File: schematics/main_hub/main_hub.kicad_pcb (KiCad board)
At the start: 2 copper layers, 23 parts, among them J1 Conn_02x25_Counter_Clockwise, J2 Conn_02x25_Counter_Clockwise, J3 Conn_02x25_Counter_Clockwise, J4 Conn_02x25_Counter_Clockwise

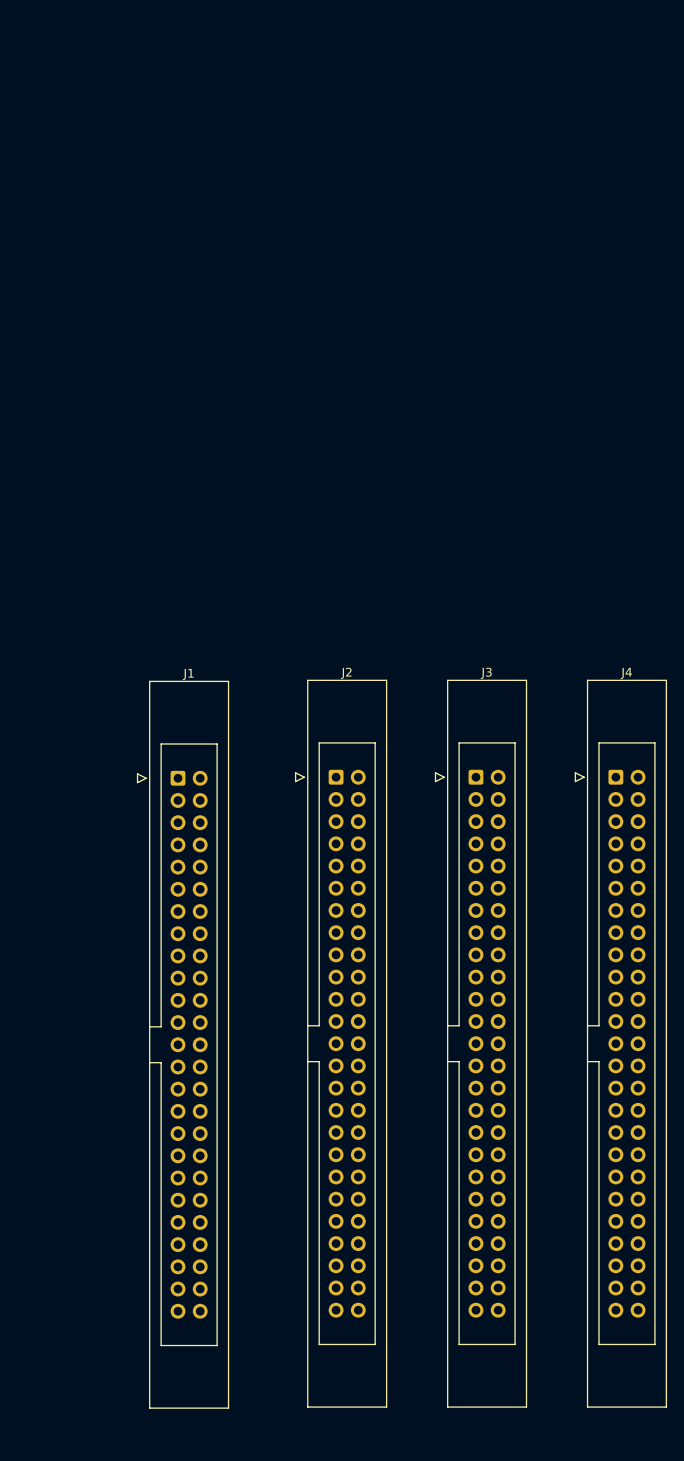
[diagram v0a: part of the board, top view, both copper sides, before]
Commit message: Add more labels to main hub decoder
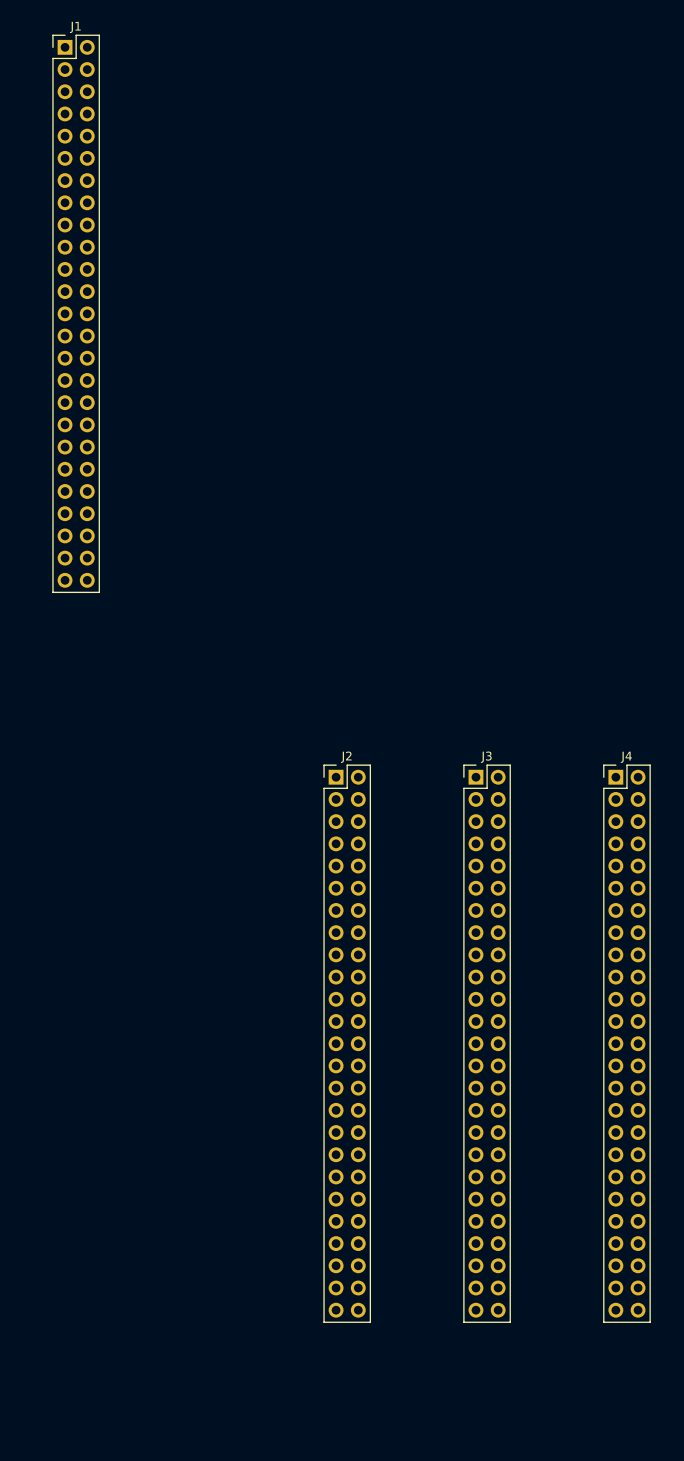
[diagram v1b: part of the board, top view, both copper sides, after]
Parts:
- J1, J2, J3, J4: footprint Connector_IDC:IDC-Header_2x25_P2.54mm_Latch_Vertical -> Connector_PinHeader_2.54mm:PinHeader_2x25_P2.54mm_Vertical
- moved J1 84.6 mm to (180.0, -5.48)
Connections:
- DECODER1 pad 7: unconnected-(DECODER1-S6-Pad7) -> /~{TemporaryHighReader}
- DECODER1 pad 9: unconnected-(DECODER1-S8-Pad9) -> /~{AccumReader}
- DECODER3 pad 7: unconnected-(DECODER3-S6-Pad7) -> /~{TemporaryHighWriter}
- DECODER3 pad 9: unconnected-(DECODER3-S8-Pad9) -> /~{AccumWriter}
- DECODER4 pad 1: unconnected-(DECODER4-S0-Pad1) -> /~{ALUWriter}
- J1 pad 1: /~{Halt} -> VCC
- J1 pad 10: unconnected-(J1-Pin_10-Pad10) -> GND
- J1 pad 2: VCC -> GND
- J1 pad 26: unconnected-(J1-Pin_26-Pad26) -> VCC
- J1 pad 27: unconnected-(J1-Pin_27-Pad27) -> /AccumWriter
- J1 pad 28: unconnected-(J1-Pin_28-Pad28) -> /AccumShiftRight
- J1 pad 29: unconnected-(J1-Pin_29-Pad29) -> /AccumShiftLeft
- J1 pad 3: /~{Reset} -> /~{Clk}
- J1 pad 30: unconnected-(J1-Pin_30-Pad30) -> /~{ALUCarryIn}
- J1 pad 31: unconnected-(J1-Pin_31-Pad31) -> /ALUM
- J1 pad 32: unconnected-(J1-Pin_32-Pad32) -> /ALUS3
- J1 pad 33: unconnected-(J1-Pin_33-Pad33) -> /ALUS2
- J1 pad 34: unconnected-(J1-Pin_34-Pad34) -> /ALUS1
- J1 pad 35: unconnected-(J1-Pin_35-Pad35) -> /ALUS0
- J1 pad 36: unconnected-(J1-Pin_36-Pad36) -> /ALUZeroOut
- J1 pad 37: unconnected-(J1-Pin_37-Pad37) -> /~{ALUCarryOut}
- J1 pad 38: unconnected-(J1-Pin_38-Pad38) -> /ALUSignOut
- J1 pad 39: unconnected-(J1-Pin_39-Pad39) -> /~{ALUWriter}
- J1 pad 4: GND -> /Clk
- J1 pad 40: unconnected-(J1-Pin_40-Pad40) -> /TemporaryHighReader
- J1 pad 41: unconnected-(J1-Pin_41-Pad41) -> /~{TemporaryHighWriter}
- J1 pad 46: unconnected-(J1-Pin_46-Pad46) -> /AccumReader
- J1 pad 48: unconnected-(J1-Pin_48-Pad48) -> /Pulse
- J1 pad 49: unconnected-(J1-Pin_49-Pad49) -> GND
- J1 pad 5: /~{Clk} -> unconnected-(J1-Pin_5-Pad5)
- J1 pad 50: unconnected-(J1-Pin_50-Pad50) -> VCC
- J1 pad 6: /Clk -> unconnected-(J1-Pin_6-Pad6)
- J2 pad 1: /~{Halt} -> VCC
- J2 pad 10: unconnected-(J2-Pin_10-Pad10) -> GND
- J2 pad 2: VCC -> GND
- J2 pad 26: unconnected-(J2-Pin_26-Pad26) -> VCC
- J2 pad 3: /~{Reset} -> /~{Clk}
- J2 pad 4: GND -> /Clk
- J2 pad 48: unconnected-(J2-Pin_48-Pad48) -> /Pulse
- J2 pad 49: unconnected-(J2-Pin_49-Pad49) -> GND
- J2 pad 5: /~{Clk} -> unconnected-(J2-Pin_5-Pad5)
- J2 pad 50: unconnected-(J2-Pin_50-Pad50) -> VCC
- J2 pad 6: /Clk -> unconnected-(J2-Pin_6-Pad6)
- J3 pad 1: /~{Halt} -> VCC
- J3 pad 10: unconnected-(J3-Pin_10-Pad10) -> GND
- J3 pad 2: VCC -> GND
- J3 pad 26: unconnected-(J3-Pin_26-Pad26) -> VCC
- J3 pad 3: /~{Reset} -> /~{Clk}
- J3 pad 4: GND -> /Clk
- J3 pad 48: unconnected-(J3-Pin_48-Pad48) -> /Pulse
- J3 pad 49: unconnected-(J3-Pin_49-Pad49) -> GND
- J3 pad 5: /~{Clk} -> unconnected-(J3-Pin_5-Pad5)
- J3 pad 50: unconnected-(J3-Pin_50-Pad50) -> VCC
- J3 pad 6: /Clk -> unconnected-(J3-Pin_6-Pad6)
- J4 pad 1: /~{Halt} -> VCC
- J4 pad 10: unconnected-(J4-Pin_10-Pad10) -> GND
- J4 pad 2: VCC -> GND
- J4 pad 26: unconnected-(J4-Pin_26-Pad26) -> VCC
- J4 pad 3: /~{Reset} -> /~{Clk}
- J4 pad 4: GND -> /Clk
- J4 pad 48: unconnected-(J4-Pin_48-Pad48) -> /Pulse
- J4 pad 49: unconnected-(J4-Pin_49-Pad49) -> GND
- J4 pad 5: /~{Clk} -> unconnected-(J4-Pin_5-Pad5)
- J4 pad 50: unconnected-(J4-Pin_50-Pad50) -> VCC
- J4 pad 6: /Clk -> unconnected-(J4-Pin_6-Pad6)
- NOT2 pad 10: unconnected-(NOT2-Pad10) -> /AccumReader
- NOT2 pad 11: unconnected-(NOT2-Pad11) -> /~{AccumReader}
- NOT2 pad 12: unconnected-(NOT2-Pad12) -> /TemporaryHighReader
- NOT2 pad 13: unconnected-(NOT2-Pad13) -> /~{TemporaryHighReader}
- NOT2 pad 8: unconnected-(NOT2-Pad8) -> /AccumWriter
- NOT2 pad 9: unconnected-(NOT2-Pad9) -> /~{AccumWriter}
- TABLE1 pad 17: Net-(TABLE1-D5) -> /ALUM
- TABLE1 pad 18: Net-(TABLE1-D6) -> /~{ALUCarryIn}
- TABLE2 pad 17: Net-(TABLE1-D5) -> /ALUM
- TABLE2 pad 18: Net-(TABLE1-D6) -> /~{ALUCarryIn}
- TABLE5 pad 11: Net-(TABLE5-D0) -> /ALUS0
- TABLE5 pad 12: Net-(TABLE5-D1) -> /ALUS1
- TABLE5 pad 13: Net-(TABLE5-D2) -> /ALUS2
- TABLE5 pad 15: Net-(TABLE5-D3) -> /ALUS3
- TABLE5 pad 18: Net-(TABLE5-D6) -> /AccumShiftLeft
- TABLE5 pad 19: Net-(TABLE5-D7) -> /AccumShiftRight
- TABLE6 pad 11: Net-(TABLE5-D0) -> /ALUS0
- TABLE6 pad 12: Net-(TABLE5-D1) -> /ALUS1
- TABLE6 pad 13: Net-(TABLE5-D2) -> /ALUS2
- TABLE6 pad 15: Net-(TABLE5-D3) -> /ALUS3
- TABLE6 pad 18: Net-(TABLE5-D6) -> /AccumShiftLeft
- TABLE6 pad 19: Net-(TABLE5-D7) -> /AccumShiftRight
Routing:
- net Net-(TABLE1-D5): track 41.9 -> 0.00 mm
- net /ALUM: track 0.00 -> 41.9 mm
- net Net-(TABLE1-D6): track 41.2 -> 0.00 mm
- net /~{ALUCarryIn}: track 0.00 -> 41.2 mm
- net Net-(TABLE5-D3): track 40.0 -> 0.00 mm
- net /ALUS3: track 0.00 -> 40.0 mm
- net Net-(TABLE5-D0): track 39.7 -> 0.00 mm
- net /ALUS0: track 0.00 -> 39.7 mm
- net Net-(TABLE5-D1): track 39.7 -> 0.00 mm
- net /ALUS1: track 0.00 -> 39.7 mm

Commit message: Connnect all modules together
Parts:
- added U1: 74LS02, Package_DIP:DIP-14_W7.62mm_Socket_LongPads, F.Cu at (111.4, 15.8)
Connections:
- net Net-(TABLE3-D7) renamed /PCIncrement
- net Net-(TABLE5-D4) renamed /SPDecrement
- net Net-(TABLE5-D5) renamed /SPIncrement
- net Net-(TABLE7-D2) renamed /AddrDecrement
- net Net-(TABLE7-D3) renamed /AddrIncrement
- DECODER1 pad 10: unconnected-(DECODER1-S9-Pad10) -> /~{XHReader}
- DECODER1 pad 11: unconnected-(DECODER1-S10-Pad11) -> /~{YLReader}
- DECODER1 pad 13: unconnected-(DECODER1-S11-Pad13) -> /~{YHReader}
- DECODER1 pad 14: unconnected-(DECODER1-S12-Pad14) -> /~{ZLReader}
- DECODER1 pad 15: unconnected-(DECODER1-S13-Pad15) -> /~{ZHReader}
- DECODER1 pad 16: unconnected-(DECODER1-S14-Pad16) -> /~{FlagsReader}
- DECODER1 pad 17: unconnected-(DECODER1-S15-Pad17) -> /~{InstructionReader}
- DECODER1 pad 2: unconnected-(DECODER1-S1-Pad2) -> /~{MemoryReader}
- DECODER1 pad 3: unconnected-(DECODER1-S2-Pad3) -> /~{SPHighReader}
- DECODER1 pad 4: unconnected-(DECODER1-S3-Pad4) -> /~{SPLowReader}
- DECODER1 pad 5: unconnected-(DECODER1-S4-Pad5) -> /~{PCHighReader}
- DECODER1 pad 6: unconnected-(DECODER1-S5-Pad6) -> /~{PCLowReader}
- DECODER1 pad 8: unconnected-(DECODER1-S7-Pad8) -> /~{TemporaryLowReader}
- DECODER2 pad 1: unconnected-(DECODER2-S0-Pad1) -> /~{AddressHighReader}
- DECODER2 pad 2: unconnected-(DECODER2-S1-Pad2) -> /~{AddressLowReader}
- DECODER3 pad 10: unconnected-(DECODER3-S9-Pad10) -> /~{XHWriter}
- DECODER3 pad 11: unconnected-(DECODER3-S10-Pad11) -> /~{YLWriter}
- DECODER3 pad 13: unconnected-(DECODER3-S11-Pad13) -> /~{YHWriter}
- DECODER3 pad 14: unconnected-(DECODER3-S12-Pad14) -> /~{ZLWriter}
- DECODER3 pad 15: unconnected-(DECODER3-S13-Pad15) -> /~{ZHWriter}
- DECODER3 pad 16: unconnected-(DECODER3-S14-Pad16) -> /~{FlagsWriter}
- DECODER3 pad 17: unconnected-(DECODER3-S15-Pad17) -> /~{ConstantWriter}
- DECODER3 pad 2: unconnected-(DECODER3-S1-Pad2) -> /~{MemoryWriter}
- DECODER3 pad 3: unconnected-(DECODER3-S2-Pad3) -> /~{SPHighWriter}
- DECODER3 pad 4: unconnected-(DECODER3-S3-Pad4) -> /~{SPLowWriter}
- DECODER3 pad 5: unconnected-(DECODER3-S4-Pad5) -> /~{PCHighWriter}
- DECODER3 pad 6: unconnected-(DECODER3-S5-Pad6) -> /~{PCLowWriter}
- DECODER3 pad 8: unconnected-(DECODER3-S7-Pad8) -> /~{TemporaryLowWriter}
- DECODER4 pad 2: unconnected-(DECODER4-S1-Pad2) -> /~{IntAck}
- INSTRUCTION1 pad 11: /Clk -> Net-(INSTRUCTION1-Cp)
- J1 pad 27: /AccumWriter -> /~{AccumWriter}
- J1 pad 40: /TemporaryHighReader -> /~{TemporaryHighReader}
- J1 pad 46: /AccumReader -> /~{AccumReader}
- J2 pad 21: unconnected-(J2-Pin_21-Pad21) -> /ALUZeroOut
- J2 pad 22: unconnected-(J2-Pin_22-Pad22) -> /~{ALUCarryOut}
- J2 pad 23: unconnected-(J2-Pin_23-Pad23) -> /ALUSignOut
- J2 pad 28: unconnected-(J2-Pin_28-Pad28) -> /~{FlagsUpdate}
- J2 pad 29: unconnected-(J2-Pin_29-Pad29) -> /~{ZHReader}
- J2 pad 30: unconnected-(J2-Pin_30-Pad30) -> /~{ZLReader}
- J2 pad 31: unconnected-(J2-Pin_31-Pad31) -> /~{YHReader}
- J2 pad 32: unconnected-(J2-Pin_32-Pad32) -> /~{YLReader}
- J2 pad 33: unconnected-(J2-Pin_33-Pad33) -> /~{XHReader}
- J2 pad 34: unconnected-(J2-Pin_34-Pad34) -> /~{FlagsReader}
- J2 pad 35: unconnected-(J2-Pin_35-Pad35) -> /~{ZHWriter}
- J2 pad 36: unconnected-(J2-Pin_36-Pad36) -> /~{ZLWriter}
- J2 pad 37: unconnected-(J2-Pin_37-Pad37) -> /~{YHWriter}
- J2 pad 38: unconnected-(J2-Pin_38-Pad38) -> /~{YLWriter}
- J2 pad 39: unconnected-(J2-Pin_39-Pad39) -> /~{XHWriter}
- J2 pad 40: unconnected-(J2-Pin_40-Pad40) -> /~{FlagsWriter}
- J2 pad 44: unconnected-(J2-Pin_44-Pad44) -> /STATE8
- J2 pad 45: unconnected-(J2-Pin_45-Pad45) -> /STATE9
- J2 pad 46: unconnected-(J2-Pin_46-Pad46) -> /STATE10
- TABLE1 pad 19: Net-(TABLE1-D7) -> /~{FlagsUpdate}
- TABLE2 pad 19: Net-(TABLE1-D7) -> /~{FlagsUpdate}

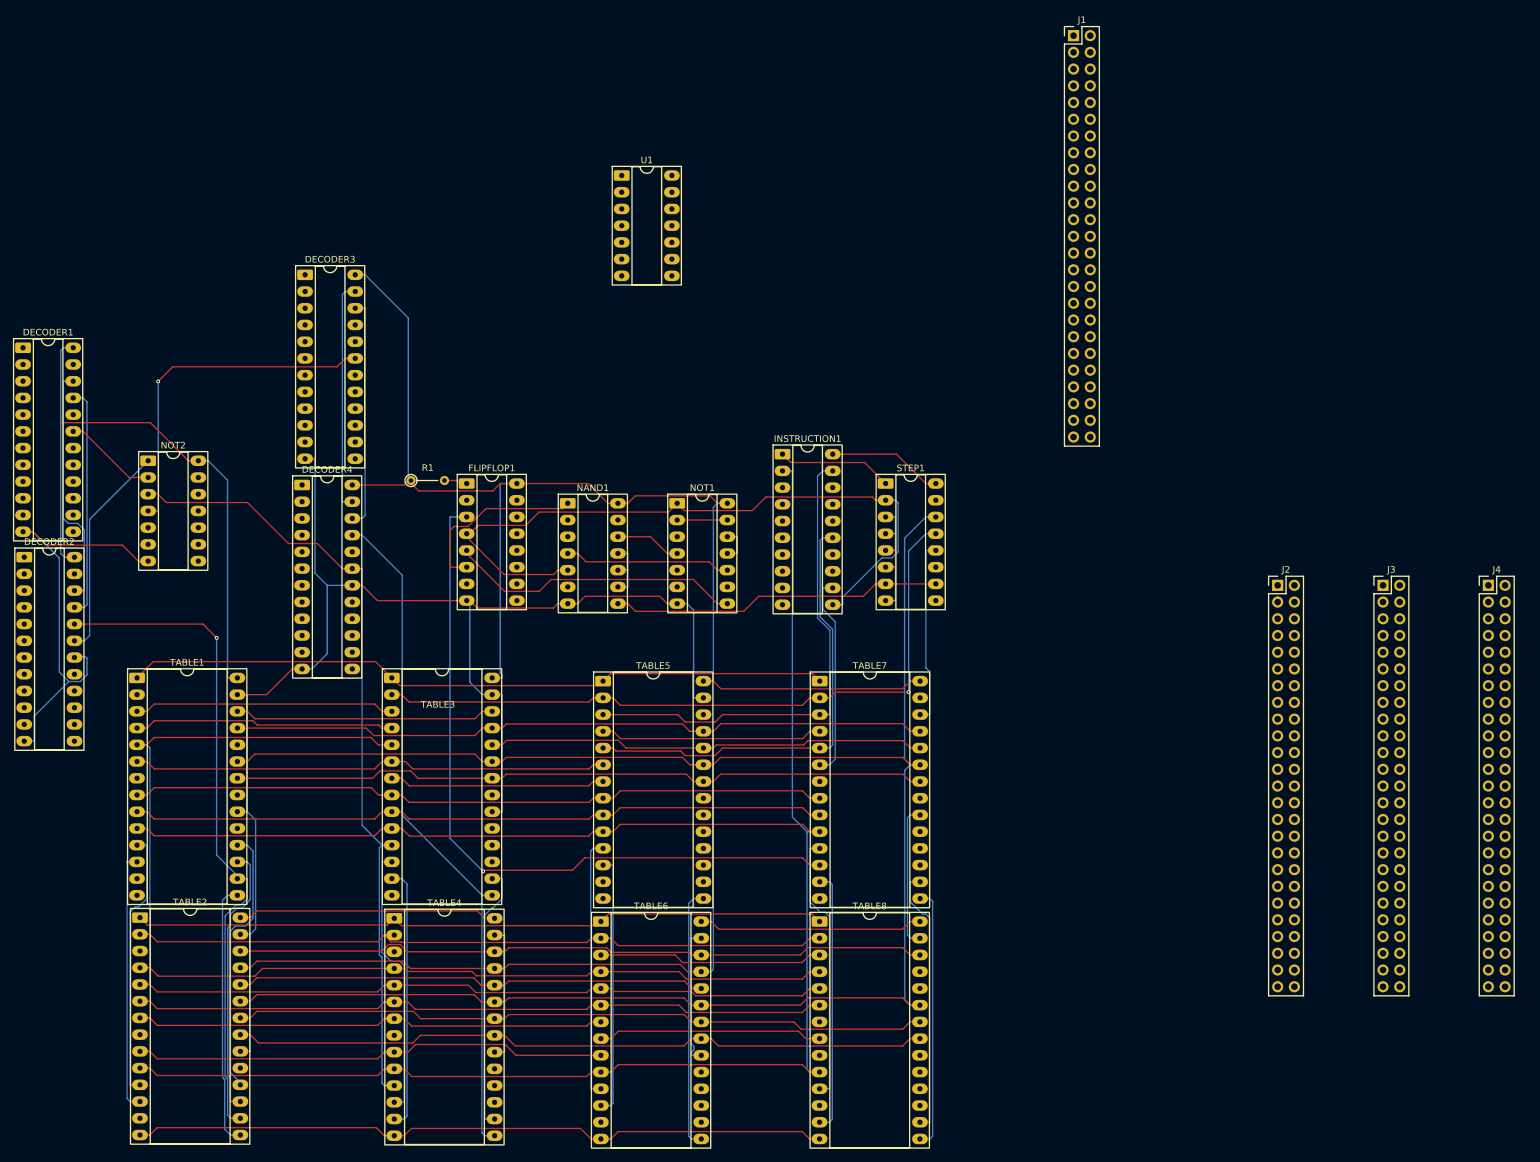
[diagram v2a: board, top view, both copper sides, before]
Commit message: Add interface module schematic
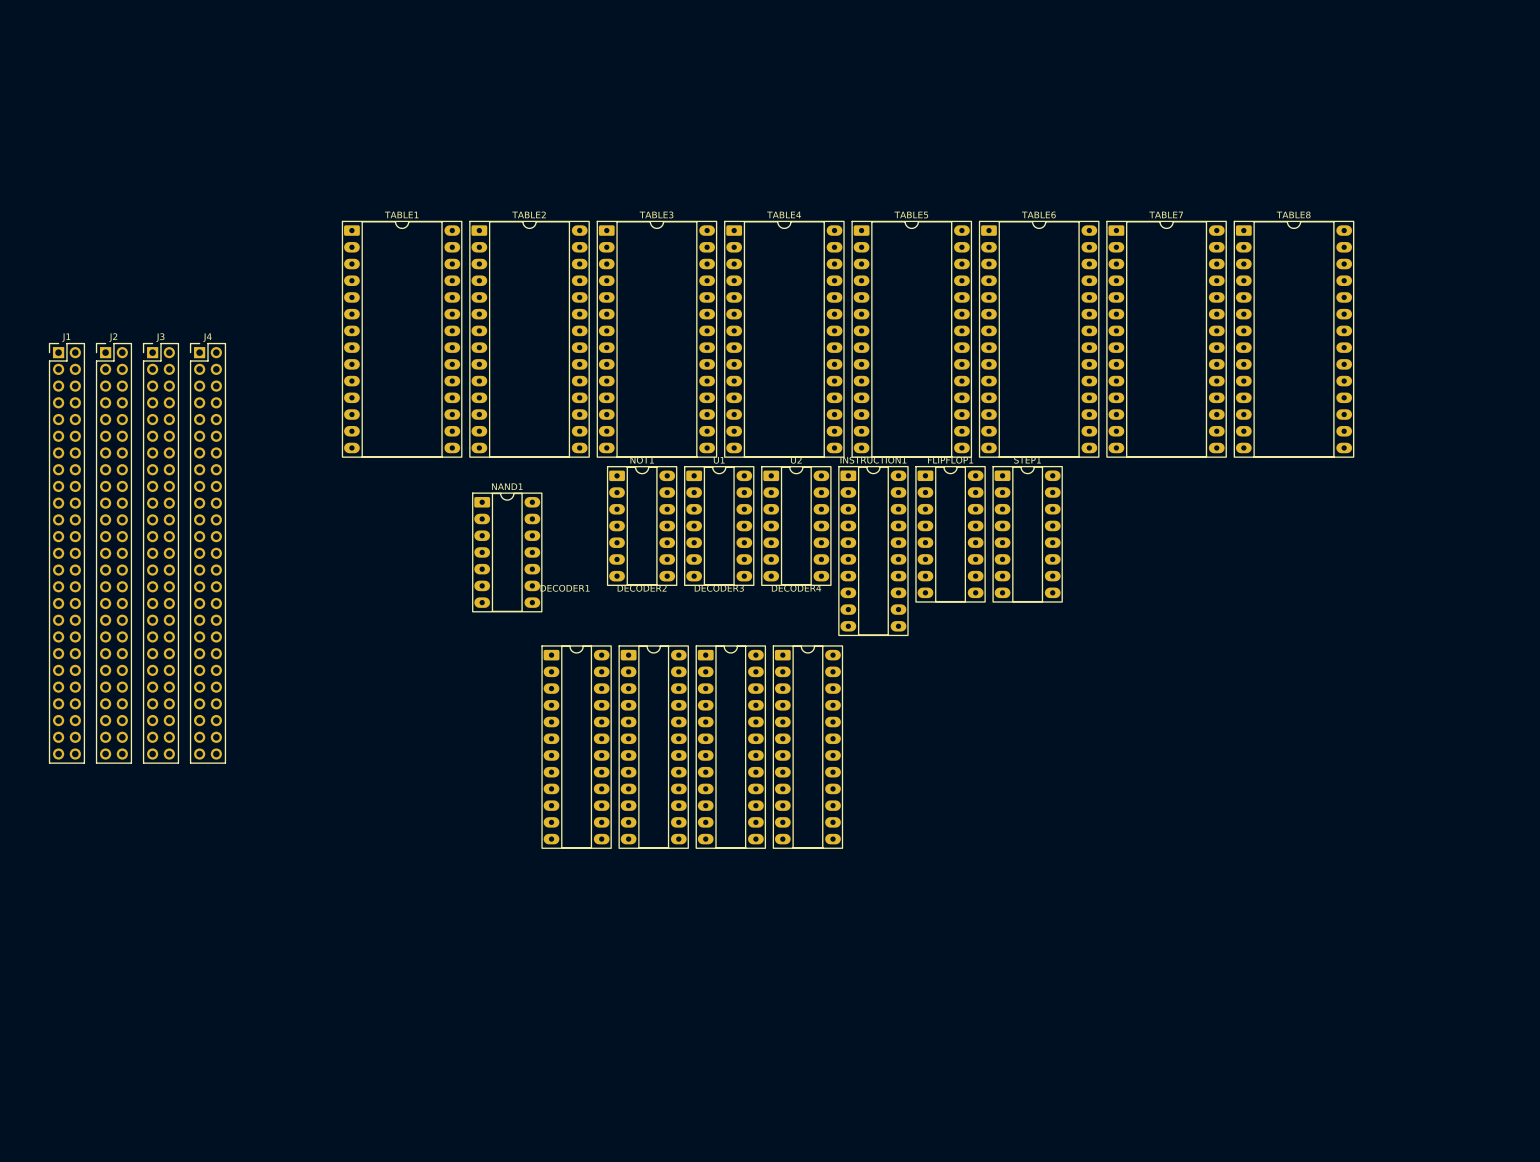
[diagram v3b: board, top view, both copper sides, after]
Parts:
- removed NOT2: 74LS04, Package_DIP:DIP-14_W7.62mm_Socket_LongPads
- removed R1: 5kOhm, Resistor_THT:R_Axial_DIN0204_L3.6mm_D1.6mm_P5.08mm_Vertical
- added U2: 74LS04, Package_DIP:DIP-14_W7.62mm_Socket_LongPads, F.Cu at (134.1, 61.4)
- moved J4 198.9 mm to (47.3, 42.7)
- moved J3 190.2 mm to (40.1, 42.7)
- moved J2 181.5 mm to (33.0, 42.7)
- moved J1 161.5 mm to (25.9, 42.7)
- moved TABLE8 123.1 mm to (205.9, 24.1)
- moved TABLE6 120.4 mm to (167.2, 24.1)
- moved TABLE4 116.5 mm to (128.5, 24.1)
- moved TABLE2 116.4 mm to (89.8, 24.1)
- moved DECODER2 93.0 mm to (112.4, 88.6)
- moved DECODER1 92.8 mm to (100.7, 88.6)
- moved DECODER3 83.9 mm to (124.1, 88.6)
- moved TABLE7 81.9 mm to (186.5, 24.1)
- moved TABLE5 78.9 mm to (147.8, 24.1)
- moved DECODER4 77.4 mm to (135.8, 88.6)
- moved TABLE1 75.4 mm to (70.4, 24.1)
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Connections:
- J3 pad 34: unconnected-(J3-Pin_34-Pad34) -> /Reset
- J3 pad 35: unconnected-(J3-Pin_35-Pad35) -> /IntAck
- J3 pad 36: unconnected-(J3-Pin_36-Pad36) -> /IntReq
- J3 pad 37: unconnected-(J3-Pin_37-Pad37) -> /Wait
- J3 pad 38: unconnected-(J3-Pin_38-Pad38) -> /Halt
- J3 pad 39: unconnected-(J3-Pin_39-Pad39) -> /MemRead
- J3 pad 40: unconnected-(J3-Pin_40-Pad40) -> /MemWrite
- J3 pad 44: unconnected-(J3-Pin_44-Pad44) -> /AddrDec
- J3 pad 45: unconnected-(J3-Pin_45-Pad45) -> /AddrInc
- J3 pad 46: unconnected-(J3-Pin_46-Pad46) -> /AddrLowIn
- J3 pad 47: unconnected-(J3-Pin_47-Pad47) -> /AddrHighIn
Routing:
- net GND: track 482.7 -> 0.00 mm
- net VCC: track 381.0 -> 0.00 mm, vias 1 -> 0
- net /STATE0: track 309.4 -> 0.00 mm
- net /STATE11: track 293.0 -> 0.00 mm
- net /STATE5: track 254.9 -> 0.00 mm
- net /STATE8: track 217.6 -> 0.00 mm
- net /STATE12: track 214.4 -> 0.00 mm, vias 1 -> 0
- net /STATE14: track 213.2 -> 0.00 mm
- net /STATE4: track 209.2 -> 0.00 mm
- net /STATE6: track 179.3 -> 0.00 mm
- net /STATE1: track 178.3 -> 0.00 mm
- net /STATE13: track 173.5 -> 0.00 mm
- net /STATE7: track 148.8 -> 0.00 mm
- net /STATE2: track 140.4 -> 0.00 mm
- net /STATE9: track 138.3 -> 0.00 mm
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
